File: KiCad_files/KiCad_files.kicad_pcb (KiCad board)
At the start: 2 copper layers, 82 x 102 mm, 74 parts, among them J1 Conn_01x02_Socket, J2 L717HDE15P, J3 Conn_01x03_Socket, SW1 WE430182070816, U1 LM22670QMR-5.0, U2 MC33275ST-3.3T3G, U3 ADM3488ExR, U6 LT1789

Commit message: fixed J3
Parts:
- moved MB1_part1 192.4 mm to (187.4, 88.3), turned to 90 degrees
- moved MB2_part1 184.9 mm to (187.4, 117.3), turned to 90 degrees
- moved MB1_part2 172.7 mm to (187.4, 65.8), turned to 90 degrees
- moved MB2_part2 162.2 mm to (187.4, 94.8), turned to 90 degrees
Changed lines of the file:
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@@
 	(footprint "Library:MB1x8Pins"
 		(layer "F.Cu")
-		(at 35.98 11.16)
+		(at 187.38 117.34 90)
 		(property "Reference" "MB2_part1"
-			(at 0 -0.5 0)
+			(at 0 -0.5 90)
 			(unlocked yes)
 			(layer "F.SilkS")
@@
 		)
 		(property "Value" "Conn_01x08_Pin"
-			(at 0 1 0)
+			(at 0 1 90)
 			(unlocked yes)
 			(layer "F.Fab")
@@
 		)
 		(property "Footprint" "Library:MB1x8Pins"
-			(at 0 0 0)
+			(at 0 0 90)
 			(unlocked yes)
 			(layer "F.Fab")
@@
 		)
 		(property "Datasheet" ""
-			(at 0 0 0)
+			(at 0 0 90)
 			(unlocked yes)
 			(layer "F.Fab")
@@
 		)
 		(property "Description" "Generic connector, single row, 01x08, script generated"
-			(at 0 0 0)
+			(at 0 0 90)
 			(unlocked yes)
 			(layer "F.Fab")
@@
 		(attr through_hole)
 		(fp_text user "${REFERENCE}"
-			(at 0 2.5 0)
+			(at 0 2.5 90)
 			(unlocked yes)
 			(layer "F.Fab")
@@
 		)
 		(pad "1" thru_hole circle
-			(at -10.16 -10.16)
+			(at -10.16 -10.16 90)
 			(size 2 2)
 			(drill 1)
@@
 		)
 		(pad "2" thru_hole circle
-			(at -10.16 -7.62)
+			(at -10.16 -7.62 90)
 			(size 2 2)
 			(drill 1)
@@
 		)
 		(pad "3" thru_hole circle
-			(at -10.16 -5.08)
+			(at -10.16 -5.08 90)
 			(size 2 2)
 			(drill 1)
@@
 		)
 		(pad "4" thru_hole circle
-			(at -10.16 -2.54)
+			(at -10.16 -2.54 90)
 			(size 2 2)
 			(drill 1)
@@
 		)
 		(pad "5" thru_hole circle
-			(at -10.16 0)
+			(at -10.16 0 90)
 			(size 2 2)
 			(drill 1)
@@
 		)
 		(pad "6" thru_hole circle
-			(at -10.16 2.54)
+			(at -10.16 2.54 90)
 			(size 2 2)
 			(drill 1)
@@
 		)
 		(pad "7" thru_hole circle
-			(at -10.16 5.08)
+			(at -10.16 5.08 90)
 			(size 2 2)
 			(drill 1)
@@
 		)
 		(pad "8" thru_hole circle
-			(at -10.16 7.62)
+			(at -10.16 7.62 90)
 			(size 2 2)
 			(drill 1)
@@
 	(footprint "Library:MB1x8Pins_part2"
 		(layer "F.Cu")
-		(at 23.57 11.16)
+		(at 187.38 65.84 90)
 		(property "Reference" "MB1_part2"
-			(at 0 -0.5 0)
+			(at 0 -0.5 90)
 			(unlocked yes)
 			(layer "F.SilkS")
@@
 		)
 		(property "Value" "Conn_01x08_Pin"
-			(at 0 1 0)
+			(at 0 1 90)
 			(unlocked yes)
 			(layer "F.Fab")
@@
 		)
 		(property "Footprint" "Library:MB1x8Pins_part2"
-			(at 0 0 0)
+			(at 0 0 90)
 			(unlocked yes)
 			(layer "F.Fab")
@@
 		)
 		(property "Datasheet" ""
-			(at 0 0 0)
+			(at 0 0 90)
 			(unlocked yes)
 			(layer "F.Fab")
@@
 		)
 		(property "Description" "Generic connector, single row, 01x08, script generated"
-			(at 0 0 0)
+			(at 0 0 90)
 			(unlocked yes)
 			(layer "F.Fab")
@@
 		(attr through_hole)
 		(fp_text user "${REFERENCE}"
-			(at 0 2.5 0)
+			(at 0 2.5 90)
 			(unlocked yes)
 			(layer "F.Fab")
@@
 		)
 		(pad "9" thru_hole circle
-			(at -10.16 7.62)
+			(at -10.16 7.62 90)
 			(size 2 2)
 			(drill 1)
@@
 		)
 		(pad "10" thru_hole circle
-			(at -10.16 5.08)
+			(at -10.16 5.08 90)
 			(size 2 2)
 			(drill 1)
@@
 		)
 		(pad "11" thru_hole circle
-			(at -10.16 2.54)
+			(at -10.16 2.54 90)
 			(size 2 2)
 			(drill 1)
@@
 		)
 		(pad "12" thru_hole circle
-			(at -10.16 0)
+			(at -10.16 0 90)
 			(size 2 2)
 			(drill 1)
@@
 		)
 		(pad "13" thru_hole circle
-			(at -10.16 -2.54)
+			(at -10.16 -2.54 90)
 			(size 2 2)
 			(drill 1)
@@
 		)
 		(pad "14" thru_hole circle
-			(at -10.16 -5.08)
+			(at -10.16 -5.08 90)
 			(size 2 2)
 			(drill 1)
@@
 		)
 		(pad "15" thru_hole circle
-			(at -10.16 -7.62)
+			(at -10.16 -7.62 90)
 			(size 2 2)
 			(drill 1)
@@
 		)
 		(pad "16" thru_hole circle
-			(at -10.16 -10.16)
+			(at -10.16 -10.16 90)
 			(size 2 2)
 			(drill 1)
@@
 	(footprint "Library:MB1x8Pins"
 		(layer "F.Cu")
-		(at 11.16 11.16)
+		(at 187.38 88.34 90)
 		(property "Reference" "MB1_part1"
-			(at 0 -0.5 0)
+			(at 0 -0.5 90)
 			(unlocked yes)
 			(layer "F.SilkS")
@@
 		)
 		(property "Value" "Conn_01x08_Pin"
-			(at 0 1 0)
+			(at 0 1 90)
 			(unlocked yes)
 			(layer "F.Fab")
@@
 		)
 		(property "Footprint" "Library:MB1x8Pins"
-			(at 0 0 0)
+			(at 0 0 90)
 			(unlocked yes)
 			(layer "F.Fab")
@@
 		)
 		(property "Datasheet" ""
-			(at 0 0 0)
+			(at 0 0 90)
 			(unlocked yes)
 			(layer "F.Fab")
@@
 		)
 		(property "Description" "Generic connector, single row, 01x08, script generated"
-			(at 0 0 0)
+			(at 0 0 90)
 			(unlocked yes)
 			(layer "F.Fab")
@@
 		(attr through_hole)
 		(fp_text user "${REFERENCE}"
-			(at 0 2.5 0)
+			(at 0 2.5 90)
 			(unlocked yes)
 			(layer "F.Fab")
@@
 		)
 		(pad "1" thru_hole circle
-			(at -10.16 -10.16)
+			(at -10.16 -10.16 90)
 			(size 2 2)
 			(drill 1)
@@
 		)
 		(pad "2" thru_hole circle
-			(at -10.16 -7.62)
+			(at -10.16 -7.62 90)
 			(size 2 2)
 			(drill 1)
@@
 		)
 		(pad "3" thru_hole circle
-			(at -10.16 -5.08)
+			(at -10.16 -5.08 90)
 			(size 2 2)
 			(drill 1)
@@
 		)
 		(pad "4" thru_hole circle
-			(at -10.16 -2.54)
+			(at -10.16 -2.54 90)
 			(size 2 2)
 			(drill 1)
@@
 		)
 		(pad "5" thru_hole circle
-			(at -10.16 0)
+			(at -10.16 0 90)
 			(size 2 2)
 			(drill 1)
@@
 		)
 		(pad "6" thru_hole circle
-			(at -10.16 2.54)
+			(at -10.16 2.54 90)
 			(size 2 2)
 			(drill 1)
@@
 		)
 		(pad "7" thru_hole circle
-			(at -10.16 5.08)
+			(at -10.16 5.08 90)
 			(size 2 2)
 			(drill 1)
@@
 		)
 		(pad "8" thru_hole circle
-			(at -10.16 7.62)
+			(at -10.16 7.62 90)
 			(size 2 2)
 			(drill 1)
@@
 	(footprint "Library:MB1x8Pins_part2"
 		(layer "F.Cu")
-		(at 48.39 11.16)
+		(at 187.38 94.84 90)
 		(property "Reference" "MB2_part2"
-			(at 0 -0.5 0)
+			(at 0 -0.5 90)
 			(unlocked yes)
 			(layer "F.SilkS")
@@
 		)
 		(property "Value" "Conn_01x08_Pin"
-			(at 0 1 0)
+			(at 0 1 90)
 			(unlocked yes)
 			(layer "F.Fab")
@@
 		)
 		(property "Footprint" "Library:MB1x8Pins_part2"
-			(at 0 0 0)
+			(at 0 0 90)
 			(unlocked yes)
 			(layer "F.Fab")
@@
 		)
 		(property "Datasheet" ""
-			(at 0 0 0)
+			(at 0 0 90)
 			(unlocked yes)
 			(layer "F.Fab")
@@
 		)
 		(property "Description" "Generic connector, single row, 01x08, script generated"
-			(at 0 0 0)
+			(at 0 0 90)
 			(unlocked yes)
 			(layer "F.Fab")
@@
 		(attr through_hole)
 		(fp_text user "${REFERENCE}"
-			(at 0 2.5 0)
+			(at 0 2.5 90)
 			(unlocked yes)
 			(layer "F.Fab")
@@
 		)
 		(pad "9" thru_hole circle
-			(at -10.16 7.62)
+			(at -10.16 7.62 90)
 			(size 2 2)
 			(drill 1)
@@
 		)
 		(pad "10" thru_hole circle
-			(at -10.16 5.08)
+			(at -10.16 5.08 90)
 			(size 2 2)
 			(drill 1)
@@
 		)
 		(pad "11" thru_hole circle
-			(at -10.16 2.54)
+			(at -10.16 2.54 90)
 			(size 2 2)
 			(drill 1)
@@
 		)
 		(pad "12" thru_hole circle
-			(at -10.16 0)
+			(at -10.16 0 90)
 			(size 2 2)
 			(drill 1)
@@
 		)
 		(pad "13" thru_hole circle
-			(at -10.16 -2.54)
+			(at -10.16 -2.54 90)
 			(size 2 2)
 			(drill 1)
@@
 		)
 		(pad "14" thru_hole circle
-			(at -10.16 -5.08)
+			(at -10.16 -5.08 90)
 			(size 2 2)
 			(drill 1)
@@
 		)
 		(pad "15" thru_hole circle
-			(at -10.16 -7.62)
+			(at -10.16 -7.62 90)
 			(size 2 2)
 			(drill 1)
@@
 		)
 		(pad "16" thru_hole circle
-			(at -10.16 -10.16)
+			(at -10.16 -10.16 90)
 			(size 2 2)
 			(drill 1)

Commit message: Updated some of the PCB
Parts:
- J3: footprint Library:Pin_Header_1x3_P2.54mm -> Library:Pin_Header_1x3_P3.5mm
- moved U2 167.2 mm to (163.3, 62.5)
- moved J1 150.0 mm to (191.1, 49.0)
- moved U6 134.1 mm to (164.0, 122.5)
- moved U3 124.6 mm to (176.5, 62.1)
- moved J3 123.6 mm to (132.0, 105.5), turned to 90 degrees
- moved J2 108.0 mm to (142.4, 45.7), turned to 180 degrees
- moved RP1 104.0 mm to (137.5, 65.0)
- moved U1 101.9 mm to (150.9, 64.2)
- moved L1 101.0 mm to (99.2, 106.5)

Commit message: Significant progress on the PCB
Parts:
- added U5: ~, Package_SO:SOIC-8_3.9x4.9mm_P1.27mm, F.Cu at (133.5, 116.0)
- RP1: footprint Library:TS53YJ203MR10 -> Library:TS53YJ
- moved JP1 190.5 mm to (177.7, 137.6)
- moved D1 165.4 mm to (167.5, 55.5)
- moved U4 158.2 mm to (158.9, 118.0)
- moved R7 153.7 mm to (172.0, 120.0)
- moved C18 149.3 mm to (166.5, 120.0)
- moved C16 148.5 mm to (165.5, 113.5)
- moved C17 146.5 mm to (160.0, 123.5)
- moved R4 145.6 mm to (184.0, 68.0)
- moved R3 143.1 mm to (174.0, 90.0)
- moved C11 142.9 mm to (151.5, 120.5)
- moved C3 142.1 mm to (159.0, 73.0)
- moved C9 141.9 mm to (164.5, 71.5)
- moved R5 141.3 mm to (171.5, 98.0)
- moved C15 139.4 mm to (154.5, 112.0)
- moved R2 139.0 mm to (170.5, 84.5)
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- renumbered R10 to R11, R11 to R12
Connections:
- J3 pad 2: GNDD -> GNDA
- JP1 pad 1: GNDD -> GNDA
- JP1 pad 2: GNDA -> GNDD
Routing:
- added copper zone on B.Cu, net GNDA
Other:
- board text added: "Analog ground area"

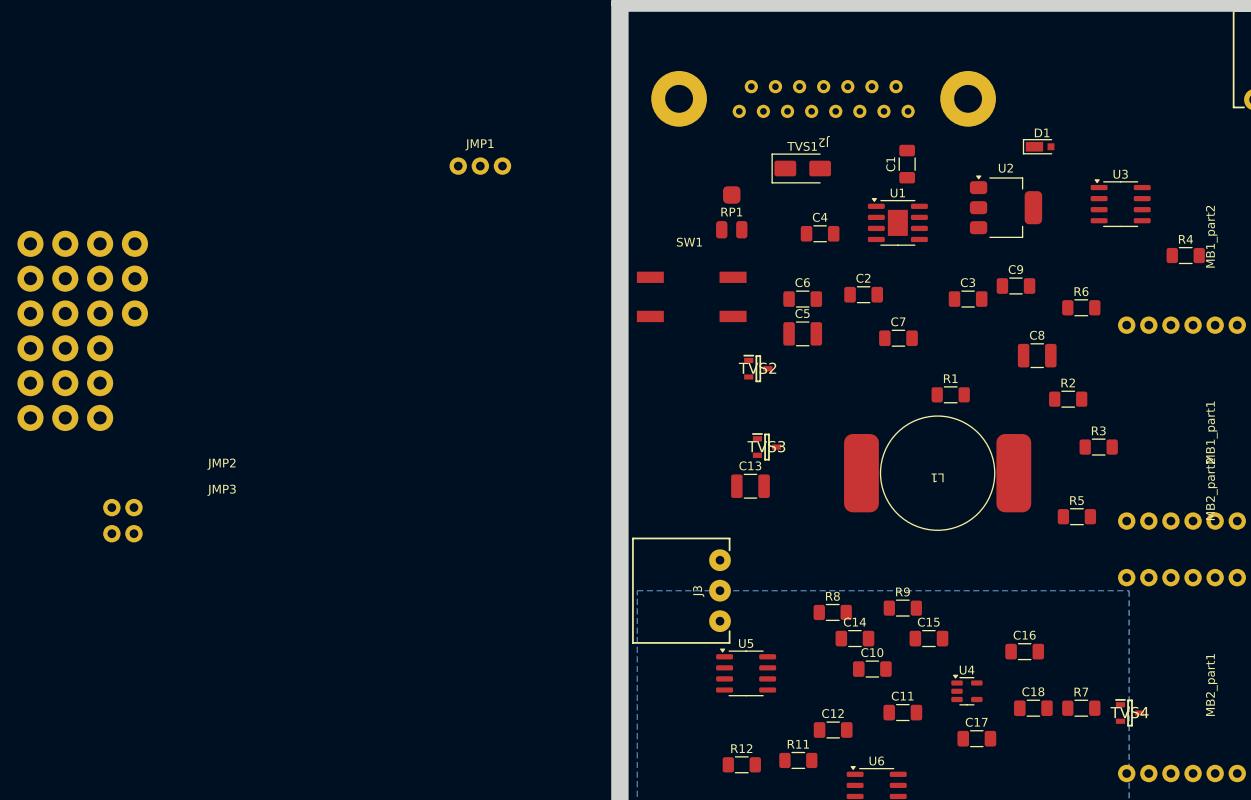
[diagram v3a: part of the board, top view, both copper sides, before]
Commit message: placed some testpoints and shortened nets
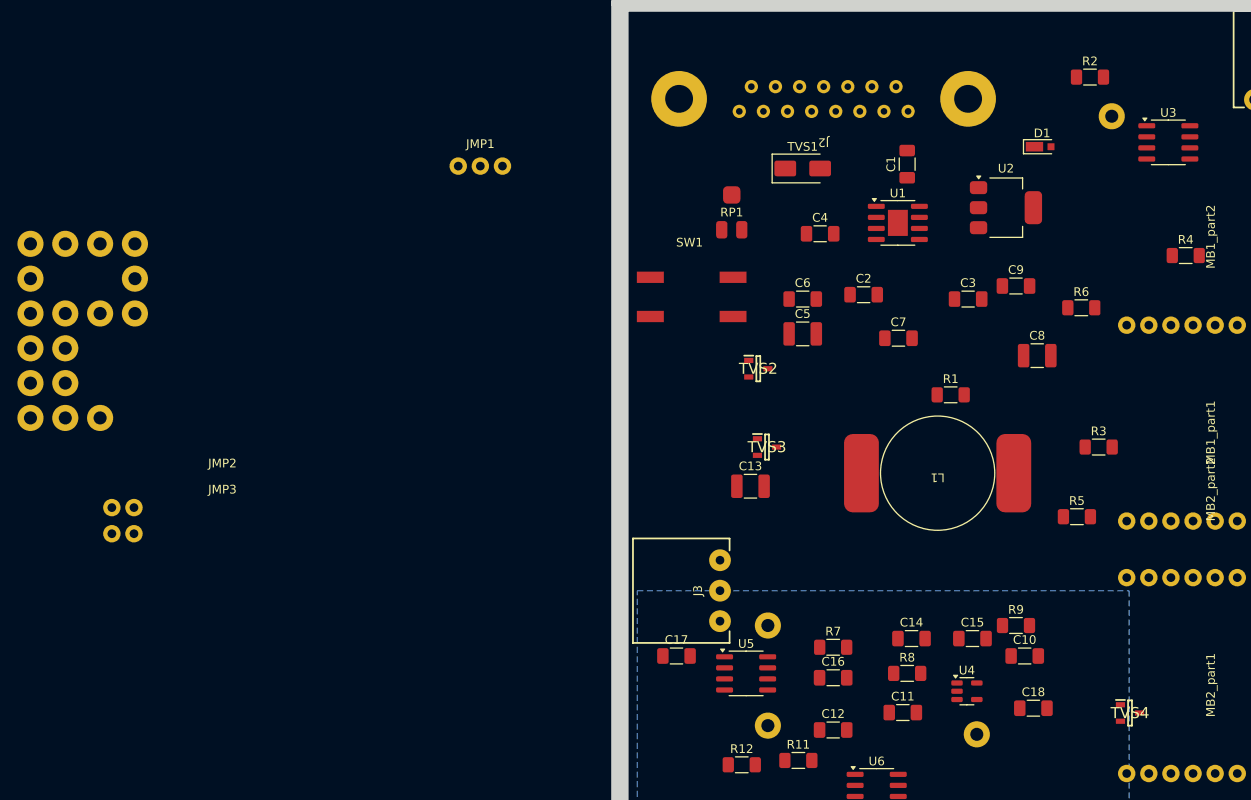
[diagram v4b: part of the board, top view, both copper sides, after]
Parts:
- moved TP5 121.6 mm to (175.5, 52.0)
- moved TP11 113.5 mm to (160.0, 123.0)
- moved TP14 86.2 mm to (136.0, 122.0)
- moved TP13 83.1 mm to (136.0, 110.5)
- moved R2 37.1 mm to (173.0, 47.5)
- moved C17 35.8 mm to (125.5, 114.0)
- moved R7 29.3 mm to (143.5, 113.0)
- moved C16 22.2 mm to (143.5, 116.5)
- moved C10 17.6 mm to (165.5, 114.0)
- moved R9 13.2 mm to (164.5, 110.5)
- moved R8 11.1 mm to (152.0, 116.0)
- moved U3 8.96 mm to (182.0, 55.0)
- moved C14 6.50 mm to (152.5, 112.0)
- moved C15 5.00 mm to (159.5, 112.0)
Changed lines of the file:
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@@
 	(footprint "Capacitor_SMD:C_1206_3216Metric_Pad1.33x1.80mm_HandSolder"
 		(layer "F.Cu")
-		(at 154.5 112)
+		(at 159.5 112)
 		(descr "Capacitor SMD 1206 (3216 Metric), square (rectangular) end terminal, IPC_7351 nominal with elongated pad for handsoldering. (Body size source: IPC-SM-782 page 76, https://www.pcb-3d.com/wordpress/wp-content/uploads/ipc-sm-782a_amendment_1_and_2.pdf), generated with kicad-footprint-generator")
 		(tags "capacitor handsolder")
@@
 	(footprint "Library:testpoint_1.4mm"
 		(layer "F.Cu")
-		(at 55.29 70.655)
+		(at 175.5 52)
 		(property "Reference" "TP5"
 			(at 0 -2 0)
@@
 	(footprint "Capacitor_SMD:C_1206_3216Metric_Pad1.33x1.80mm_HandSolder"
 		(layer "F.Cu")
-		(at 148 115.5)
+		(at 165.5 114)
 		(descr "Capacitor SMD 1206 (3216 Metric), square (rectangular) end terminal, IPC_7351 nominal with elongated pad for handsoldering. (Body size source: IPC-SM-782 page 76, https://www.pcb-3d.com/wordpress/wp-content/uploads/ipc-sm-782a_amendment_1_and_2.pdf), generated with kicad-footprint-generator")
 		(tags "capacitor handsolder")
@@
 	(footprint "Library:testpoint_1.4mm"
 		(layer "F.Cu")
-		(at 59.29 70.655)
+		(at 160 123)
 		(property "Reference" "TP11"
 			(at 0 -2 0)
@@
 	(footprint "Package_SO:SOIC-8_3.9x4.9mm_P1.27mm"
 		(layer "F.Cu")
-		(at 176.525 62.095)
+		(at 182 55)
 		(descr "SOIC, 8 Pin (JEDEC MS-012AA, https://www.analog.com/media/en/package-pcb-resources/package/pkg_pdf/soic_narrow-r/r_8.pdf), generated with kicad-footprint-generator ipc_gullwing_generator.py")
 		(tags "SOIC SO")
@@
 	(footprint "Library:testpoint_1.4mm"
 		(layer "F.Cu")
-		(at 59.29 78.655)
+		(at 136 110.5)
 		(property "Reference" "TP13"
 			(at 0 -2 0)
@@
 	(footprint "Resistor_SMD:R_1206_3216Metric_Pad1.30x1.75mm_HandSolder"
 		(layer "F.Cu")
-		(at 151.5 108.5)
+		(at 164.5 110.5)
 		(descr "Resistor SMD 1206 (3216 Metric), square (rectangular) end terminal, IPC_7351 nominal with elongated pad for handsoldering. (Body size source: IPC-SM-782 page 72, https://www.pcb-3d.com/wordpress/wp-content/uploads/ipc-sm-782a_amendment_1_and_2.pdf), generated with kicad-footprint-generator")
 		(tags "resistor handsolder")
@@
 	(footprint "Library:testpoint_1.4mm"
 		(layer "F.Cu")
-		(at 59.29 82.655)
+		(at 136 122)
 		(property "Reference" "TP14"
 			(at 0 -2 0)
@@
 	(footprint "Resistor_SMD:R_1206_3216Metric_Pad1.30x1.75mm_HandSolder"
 		(layer "F.Cu")
-		(at 172 120)
+		(at 143.5 113)
 		(descr "Resistor SMD 1206 (3216 Metric), square (rectangular) end terminal, IPC_7351 nominal with elongated pad for handsoldering. (Body size source: IPC-SM-782 page 72, https://www.pcb-3d.com/wordpress/wp-content/uploads/ipc-sm-782a_amendment_1_and_2.pdf), generated with kicad-footprint-generator")
 		(tags "resistor handsolder")
@@
 	(footprint "Capacitor_SMD:C_1206_3216Metric_Pad1.33x1.80mm_HandSolder"
 		(layer "F.Cu")
-		(at 146 112)
+		(at 152.5 112)
 		(descr "Capacitor SMD 1206 (3216 Metric), square (rectangular) end terminal, IPC_7351 nominal with elongated pad for handsoldering. (Body size source: IPC-SM-782 page 76, https://www.pcb-3d.com/wordpress/wp-content/uploads/ipc-sm-782a_amendment_1_and_2.pdf), generated with kicad-footprint-generator")
 		(tags "capacitor handsolder")
@@
 	(footprint "Resistor_SMD:R_1206_3216Metric_Pad1.30x1.75mm_HandSolder"
 		(layer "F.Cu")
-		(at 170.5 84.5)
+		(at 173 47.5)
 		(descr "Resistor SMD 1206 (3216 Metric), square (rectangular) end terminal, IPC_7351 nominal with elongated pad for handsoldering. (Body size source: IPC-SM-782 page 72, https://www.pcb-3d.com/wordpress/wp-content/uploads/ipc-sm-782a_amendment_1_and_2.pdf), generated with kicad-footprint-generator")
 		(tags "resistor handsolder")
@@
 	(footprint "Resistor_SMD:R_1206_3216Metric_Pad1.30x1.75mm_HandSolder"
 		(layer "F.Cu")
-		(at 143.45 109)
+		(at 152 116)
 		(descr "Resistor SMD 1206 (3216 Metric), square (rectangular) end terminal, IPC_7351 nominal with elongated pad for handsoldering. (Body size source: IPC-SM-782 page 72, https://www.pcb-3d.com/wordpress/wp-content/uploads/ipc-sm-782a_amendment_1_and_2.pdf), generated with kicad-footprint-generator")
 		(tags "resistor handsolder")
@@
 	(footprint "Capacitor_SMD:C_1206_3216Metric_Pad1.33x1.80mm_HandSolder"
 		(layer "F.Cu")
-		(at 165.5 113.5)
+		(at 143.5 116.5)
 		(descr "Capacitor SMD 1206 (3216 Metric), square (rectangular) end terminal, IPC_7351 nominal with elongated pad for handsoldering. (Body size source: IPC-SM-782 page 76, https://www.pcb-3d.com/wordpress/wp-content/uploads/ipc-sm-782a_amendment_1_and_2.pdf), generated with kicad-footprint-generator")
 		(tags "capacitor handsolder")
@@
 	(footprint "Capacitor_SMD:C_1206_3216Metric_Pad1.33x1.80mm_HandSolder"
 		(layer "F.Cu")
-		(at 160 123.5)
+		(at 125.5 114)
 		(descr "Capacitor SMD 1206 (3216 Metric), square (rectangular) end terminal, IPC_7351 nominal with elongated pad for handsoldering. (Body size source: IPC-SM-782 page 76, https://www.pcb-3d.com/wordpress/wp-content/uploads/ipc-sm-782a_amendment_1_and_2.pdf), generated with kicad-footprint-generator")
 		(tags "capacitor handsolder")

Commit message: Significant progress on the PCB
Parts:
- removed the TP7 at (55.3, 78.7)
- J3: moved to B.Cu
- U1: footprint Package_SO:SOIC-8-1EP_3.9x4.9mm_P1.27mm_EP2.29x3mm -> Package_SO:TI_SO-PowerPAD-8
- U2: footprint Package_TO_SOT_SMD:SOT-223 -> Package_TO_SOT_SMD:SOT-223-3_TabPin2
- moved TP1 134.8 mm to (184.0, 55.1)
- moved TGA1 128.0 mm to (165.5, 132.5)
- moved TP10 122.0 mm to (172.5, 112.0)
- moved TP9 119.2 mm to (174.5, 84.0)
- moved TG1 117.3 mm to (168.6, 67.5)
- moved JMP3 116.7 mm to (177.3, 102.5), turned to 180 degrees
- moved TP16 110.6 mm to (155.0, 128.5)
- moved TP15 109.4 mm to (160.0, 129.5)
- moved TP2 106.8 mm to (158.0, 79.5), turned to 90 degrees
- moved TP17 106.3 mm to (155.5, 123.5)
- moved JMP1 93.5 mm to (196.5, 59.6), turned to 90 degrees
- moved TP12 93.0 mm to (147.0, 105.5)
- moved TP8 92.7 mm to (147.5, 73.0)
- moved TP6 90.8 mm to (144.5, 57.5)
- moved TP3 90.1 mm to (136.5, 57.5)
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- renumbered TP18 to TP7
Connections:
- C14 pad 1: GNDA -> Net-(U5-in)
- C16 pad 1: Net-(U5-os) -> /VBIAS
- J1 pad 1: Net-(J1-Pin_1) -> /1
- J3 pad 2: GNDA -> Net-(J3-Pin_2)
- J3 pad 3: Net-(J3-Pin_2) -> GNDA
- JMP1 pad 1: unconnected-(JMP1-Pad1) -> /15
- JMP1 pad 3: Net-(J1-Pin_1) -> /1
- MB1_part2 pad 10: /MB1_10 -> +5V
- MB2_part2 pad 10: /MB1_10 -> +5V
- R11 pad 1: unconnected-(R11-Pad1) -> /VBIAS
- R9 pad 2: GNDA -> Net-(U5-in)
- RP1 pad 1: (no net) -> Net-(RP1-CCW)
- RP1 pad 2: (no net) -> Net-(RP1-WIPER)
- RP1 pad 3: (no net) -> Net-(RP1-CW)
- TP11 pad 1: Net-(U4-V_BIAS) -> /VBIAS
- U4 pad 4: Net-(U4-V_BIAS) -> /VBIAS
- U5 pad 2: GNDA -> Net-(U5-in)
- U5 pad 6: Net-(U5-os) -> /VBIAS
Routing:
- net GNDD: track 0.00 -> 89.1 mm, vias 0 -> 2
- net /15: track 0.00 -> 88.0 mm
- net /1: track 0.00 -> 61.1 mm
- net +3.3V: track 0.00 -> 51.4 mm
- net +5V: track 0.00 -> 30.4 mm
- net Net-(SW1A-C): track 0.00 -> 26.5 mm
- net Net-(D1-K): track 0.00 -> 20.3 mm, vias 0 -> 2
- net /11: track 0.00 -> 19.3 mm
- net /13: track 0.00 -> 19.0 mm
- net GNDA: track 0.00 -> 17.1 mm, vias 0 -> 1
- net /4: track 0.00 -> 16.8 mm
- net Net-(TVS3-CATHODE_COMPENSATION_DIODE): track 0.00 -> 14.9 mm
- net Net-(TVS1-A1): track 0.00 -> 14.5 mm
- net /5: track 0.00 -> 14.2 mm
- net /VBIAS: track 0.00 -> 9.31 mm
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- added copper zone on B.Cu, net GNDD
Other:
- board text added: "3.3V gen"
- board text added: "5V gen"
- board text added: "comm"
- board text added: "connect microbus"

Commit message: Some more progress on the PCB
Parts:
- moved C17 18.4 mm to (150.0, 111.0)
- moved RP1 15.0 mm to (145.0, 124.0)
- moved C16 13.5 mm to (156.9, 118.2), turned to -90 degrees
- moved U6 12.5 mm to (142.5, 118.5)
- moved TP16 12.1 mm to (167.0, 127.0)
- moved TP17 6.08 mm to (161.5, 124.5)
- moved TP11 0.50 mm to (166.0, 117.5)
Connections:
- C15 pad 1: +3.3V -> +3.3VA
- C18 pad 1: +3.3V -> +3.3VA
- U5 pad 4: +3.3V -> +3.3VA
- U5 pad 7: +3.3V -> +3.3VA
- U6 pad 7: +3.3V -> +3.3VA
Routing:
- net GNDA: track 17.1 -> 46.2 mm
- net +3.3VA: track 8.91 -> 34.9 mm
- net Net-(U5-clk): track 3.50 -> 24.6 mm
- net /VBIAS: track 9.31 -> 22.0 mm
- net Net-(U5-in): track 2.89 -> 12.9 mm
- net GNDD: track 89.1 -> 92.9 mm, vias 2 -> 4
- net Net-(U5-com): track 0.00 -> 3.13 mm
